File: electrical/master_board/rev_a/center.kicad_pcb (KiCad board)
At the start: 2 copper layers, 125 x 97.6 mm, 9 parts, among them CN50 HCSR04;F1X4, CN51 HCSR04LP;F1X4, CN52 HCSR04LP;F1X4, CN53 HCSR04LP;F1X4, CN54 HCSR04;F1X4, CN55 HR2_EncoderMate;2XF1X3, CN56 HR2_EncoderMate;2XF1X3, CN57 RASPI;F2X20, CN58 ST_MATE;ST_MATE

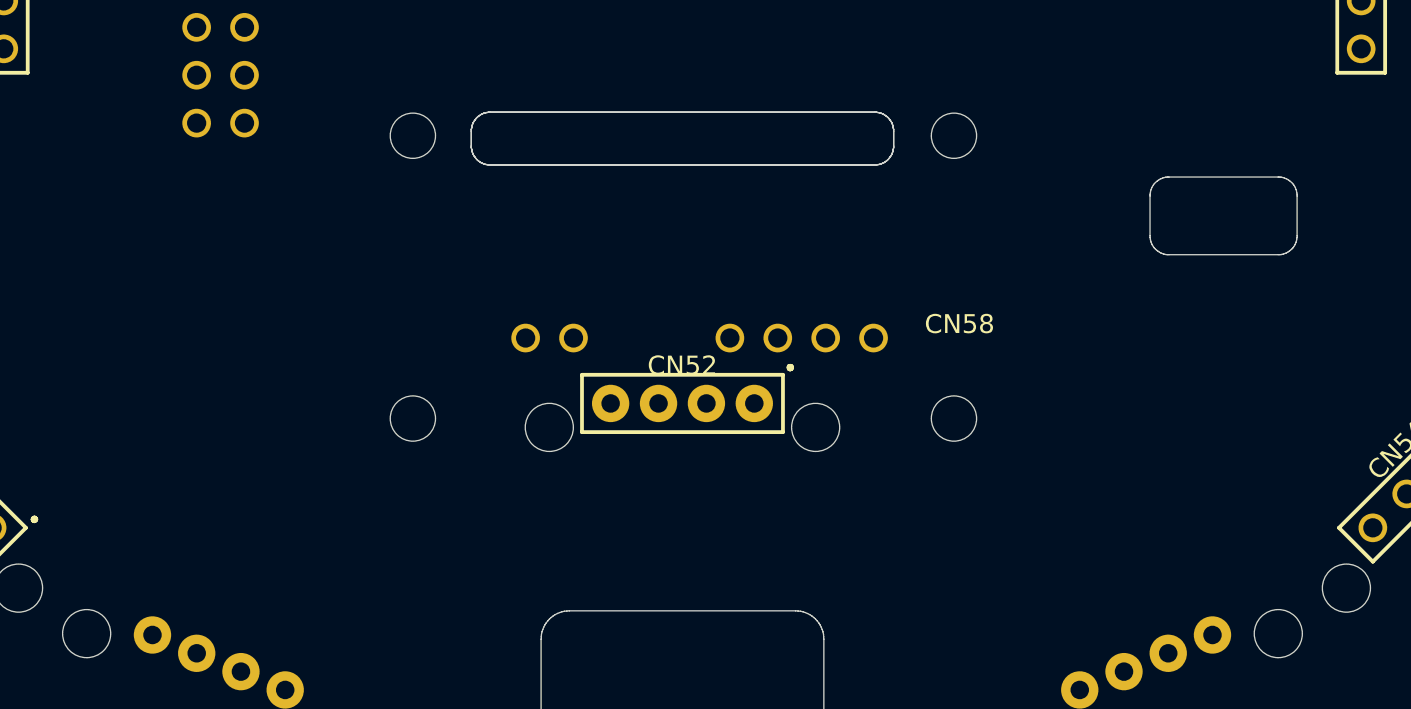
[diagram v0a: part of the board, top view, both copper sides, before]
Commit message: ST Mate is automatically placed on the center.kicad_pcb.
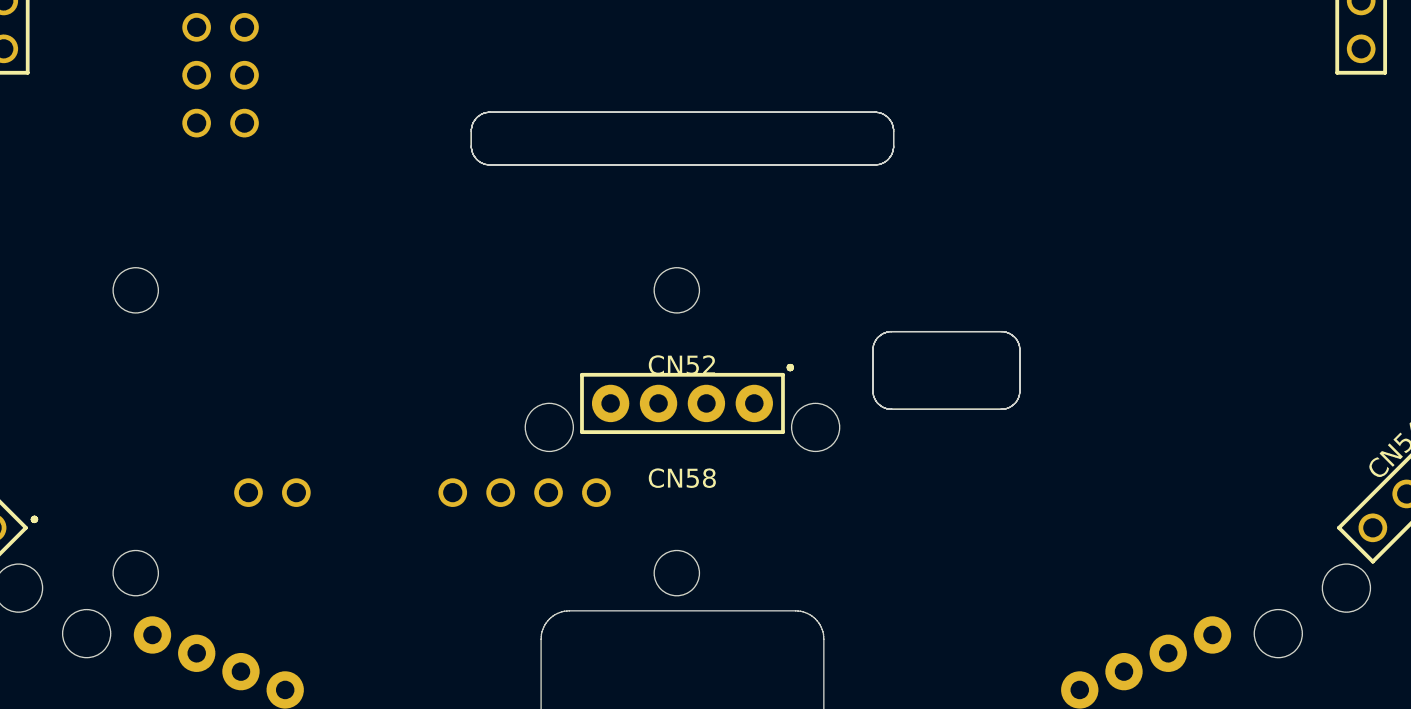
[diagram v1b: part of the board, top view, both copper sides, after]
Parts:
- moved CN58 16.8 mm to (100.0, 145.0)
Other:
- outline, holes or cut-outs redrawn
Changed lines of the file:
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@@
   )
   (module HR2:ST_MATE (layer F.Cu)
-    (at 114.7 136.8)
+    (at 100 145)
     (fp_text reference CN58 (at 0 -2) (layer F.SilkS)
       (effects (font (size 1 1) (thickness 0.2)))
@@
       (net 8 "Net-(CN52-Pad1)"))
   )
+  (gr_line (start 117.9 136.19) (end 117.9 136.1) (layer Edge.Cuts) (width 0.05))
+  (gr_line (start 117.9 136.1) (end 117.88 136.01) (layer Edge.Cuts) (width 0.05))
+  (gr_line (start 117.88 136.01) (end 117.87 135.93) (layer Edge.Cuts) (width 0.05))
+  (gr_line (start 117.87 135.93) (end 117.84 135.85) (layer Edge.Cuts) (width 0.05))
+  (gr_line (start 117.84 135.85) (end 117.81 135.76) (layer Edge.Cuts) (width 0.05))
+  (gr_line (start 117.81 135.76) (end 117.77 135.69) (layer Edge.Cuts) (width 0.05))
+  (gr_line (start 117.77 135.69) (end 117.72 135.61) (layer Edge.Cuts) (width 0.05))
+  (gr_line (start 117.72 135.61) (end 117.67 135.54) (layer Edge.Cuts) (width 0.05))
+  (gr_line (start 117.67 135.54) (end 117.61 135.48) (layer Edge.Cuts) (width 0.05))
+  (gr_line (start 117.61 135.48) (end 117.54 135.42) (layer Edge.Cuts) (width 0.05))
+  (gr_line (start 117.54 135.42) (end 117.47 135.37) (layer Edge.Cuts) (width 0.05))
+  (gr_line (start 117.47 135.37) (end 117.4 135.32) (layer Edge.Cuts) (width 0.05))
+  (gr_line (start 117.4 135.32) (end 117.32 135.28) (layer Edge.Cuts) (width 0.05))
+  (gr_line (start 117.32 135.28) (end 117.24 135.25) (layer Edge.Cuts) (width 0.05))
+  (gr_line (start 117.24 135.25) (end 117.16 135.22) (layer Edge.Cuts) (width 0.05))
+  (gr_line (start 117.16 135.22) (end 117.07 135.2) (layer Edge.Cuts) (width 0.05))
+  (gr_line (start 117.07 135.2) (end 116.99 135.19) (layer Edge.Cuts) (width 0.05))
+  (gr_line (start 116.99 135.19) (end 116.9 135.19) (layer Edge.Cuts) (width 0.05))
+  (gr_line (start 116.9 135.19) (end 111.1 135.19) (layer Edge.Cuts) (width 0.05))
+  (gr_line (start 111.1 135.19) (end 111.01 135.19) (layer Edge.Cuts) (width 0.05))
+  (gr_line (start 111.01 135.19) (end 110.93 135.2) (layer Edge.Cuts) (width 0.05))
+  (gr_line (start 110.93 135.2) (end 110.84 135.22) (layer Edge.Cuts) (width 0.05))
+  (gr_line (start 110.84 135.22) (end 110.76 135.25) (layer Edge.Cuts) (width 0.05))
+  (gr_line (start 110.76 135.25) (end 110.68 135.28) (layer Edge.Cuts) (width 0.05))
+  (gr_line (start 110.68 135.28) (end 110.6 135.32) (layer Edge.Cuts) (width 0.05))
+  (gr_line (start 110.6 135.32) (end 110.53 135.37) (layer Edge.Cuts) (width 0.05))
+  (gr_line (start 110.53 135.37) (end 110.46 135.42) (layer Edge.Cuts) (width 0.05))
+  (gr_line (start 110.46 135.42) (end 110.39 135.48) (layer Edge.Cuts) (width 0.05))
+  (gr_line (start 110.39 135.48) (end 110.33 135.54) (layer Edge.Cuts) (width 0.05))
+  (gr_line (start 110.33 135.54) (end 110.28 135.61) (layer Edge.Cuts) (width 0.05))
+  (gr_line (start 110.28 135.61) (end 110.23 135.69) (layer Edge.Cuts) (width 0.05))
+  (gr_line (start 110.23 135.69) (end 110.19 135.76) (layer Edge.Cuts) (width 0.05))
+  (gr_line (start 110.19 135.76) (end 110.16 135.85) (layer Edge.Cuts) (width 0.05))
+  (gr_line (start 110.16 135.85) (end 110.13 135.93) (layer Edge.Cuts) (width 0.05))
+  (gr_line (start 110.13 135.93) (end 110.12 136.01) (layer Edge.Cuts) (width 0.05))
+  (gr_line (start 110.12 136.01) (end 110.1 136.1) (layer Edge.Cuts) (width 0.05))
+  (gr_line (start 110.1 136.1) (end 110.1 136.19) (layer Edge.Cuts) (width 0.05))
+  (gr_line (start 110.1 136.19) (end 110.1 138.31) (layer Edge.Cuts) (width 0.05))
+  (gr_line (start 110.1 138.31) (end 110.1 138.4) (layer Edge.Cuts) (width 0.05))
+  (gr_line (start 110.1 138.4) (end 110.12 138.49) (layer Edge.Cuts) (width 0.05))
+  (gr_line (start 110.12 138.49) (end 110.13 138.57) (layer Edge.Cuts) (width 0.05))
+  (gr_line (start 110.13 138.57) (end 110.16 138.65) (layer Edge.Cuts) (width 0.05))
+  (gr_line (start 110.16 138.65) (end 110.19 138.74) (layer Edge.Cuts) (width 0.05))
+  (gr_line (start 110.19 138.74) (end 110.23 138.81) (layer Edge.Cuts) (width 0.05))
+  (gr_line (start 110.23 138.81) (end 110.28 138.89) (layer Edge.Cuts) (width 0.05))
+  (gr_line (start 110.28 138.89) (end 110.33 138.96) (layer Edge.Cuts) (width 0.05))
+  (gr_line (start 110.33 138.96) (end 110.39 139.02) (layer Edge.Cuts) (width 0.05))
+  (gr_line (start 110.39 139.02) (end 110.46 139.08) (layer Edge.Cuts) (width 0.05))
+  (gr_line (start 110.46 139.08) (end 110.53 139.13) (layer Edge.Cuts) (width 0.05))
+  (gr_line (start 110.53 139.13) (end 110.6 139.18) (layer Edge.Cuts) (width 0.05))
+  (gr_line (start 110.6 139.18) (end 110.68 139.22) (layer Edge.Cuts) (width 0.05))
+  (gr_line (start 110.68 139.22) (end 110.76 139.25) (layer Edge.Cuts) (width 0.05))
+  (gr_line (start 110.76 139.25) (end 110.84 139.28) (layer Edge.Cuts) (width 0.05))
+  (gr_line (start 110.84 139.28) (end 110.93 139.3) (layer Edge.Cuts) (width 0.05))
+  (gr_line (start 110.93 139.3) (end 111.01 139.31) (layer Edge.Cuts) (width 0.05))
+  (gr_line (start 111.01 139.31) (end 111.1 139.31) (layer Edge.Cuts) (width 0.05))
+  (gr_line (start 111.1 139.31) (end 116.9 139.31) (layer Edge.Cuts) (width 0.05))
+  (gr_line (start 116.9 139.31) (end 116.99 139.31) (layer Edge.Cuts) (width 0.05))
+  (gr_line (start 116.99 139.31) (end 117.07 139.3) (layer Edge.Cuts) (width 0.05))
+  (gr_line (start 117.07 139.3) (end 117.16 139.28) (layer Edge.Cuts) (width 0.05))
+  (gr_line (start 117.16 139.28) (end 117.24 139.25) (layer Edge.Cuts) (width 0.05))
+  (gr_line (start 117.24 139.25) (end 117.32 139.22) (layer Edge.Cuts) (width 0.05))
+  (gr_line (start 117.32 139.22) (end 117.4 139.18) (layer Edge.Cuts) (width 0.05))
+  (gr_line (start 117.4 139.18) (end 117.47 139.13) (layer Edge.Cuts) (width 0.05))
+  (gr_line (start 117.47 139.13) (end 117.54 139.08) (layer Edge.Cuts) (width 0.05))
+  (gr_line (start 117.54 139.08) (end 117.61 139.02) (layer Edge.Cuts) (width 0.05))
+  (gr_line (start 117.61 139.02) (end 117.67 138.96) (layer Edge.Cuts) (width 0.05))
+  (gr_line (start 117.67 138.96) (end 117.72 138.89) (layer Edge.Cuts) (width 0.05))
+  (gr_line (start 117.72 138.89) (end 117.77 138.81) (layer Edge.Cuts) (width 0.05))
+  (gr_line (start 117.77 138.81) (end 117.81 138.74) (layer Edge.Cuts) (width 0.05))
+  (gr_line (start 117.81 138.74) (end 117.84 138.65) (layer Edge.Cuts) (width 0.05))
+  (gr_line (start 117.84 138.65) (end 117.87 138.57) (layer Edge.Cuts) (width 0.05))
+  (gr_line (start 117.87 138.57) (end 117.88 138.49) (layer Edge.Cuts) (width 0.05))
+  (gr_line (start 117.88 138.49) (end 117.9 138.4) (layer Edge.Cuts) (width 0.05))
+  (gr_line (start 117.9 138.4) (end 117.9 138.31) (layer Edge.Cuts) (width 0.05))
+  (gr_line (start 117.9 138.31) (end 117.9 136.19) (layer Edge.Cuts) (width 0.05))
   (gr_line (start 106.3 85) (end 106.21 85) (layer Edge.Cuts) (width 0.05))
   (gr_line (start 106.21 85) (end 106.13 85.02) (layer Edge.Cuts) (width 0.05))

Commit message: Finally have everything fitting together.
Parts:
- moved CN58 17.9 mm to (117.8, 147.0)
- moved CN50 9.21 mm to (64.9, 151.1)
- moved CN54 9.21 mm to (135.1, 151.1)
- moved CN51 3.92 mm to (73.9, 149.1)
- moved CN53 3.92 mm to (126.1, 149.1)
- moved CN52 1.00 mm to (100.0, 138.0)
- moved CN55 0.30 mm to (136.3, 100.0)
- moved CN56 0.30 mm to (63.7, 100.0)
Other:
- outline, holes or cut-outs redrawn

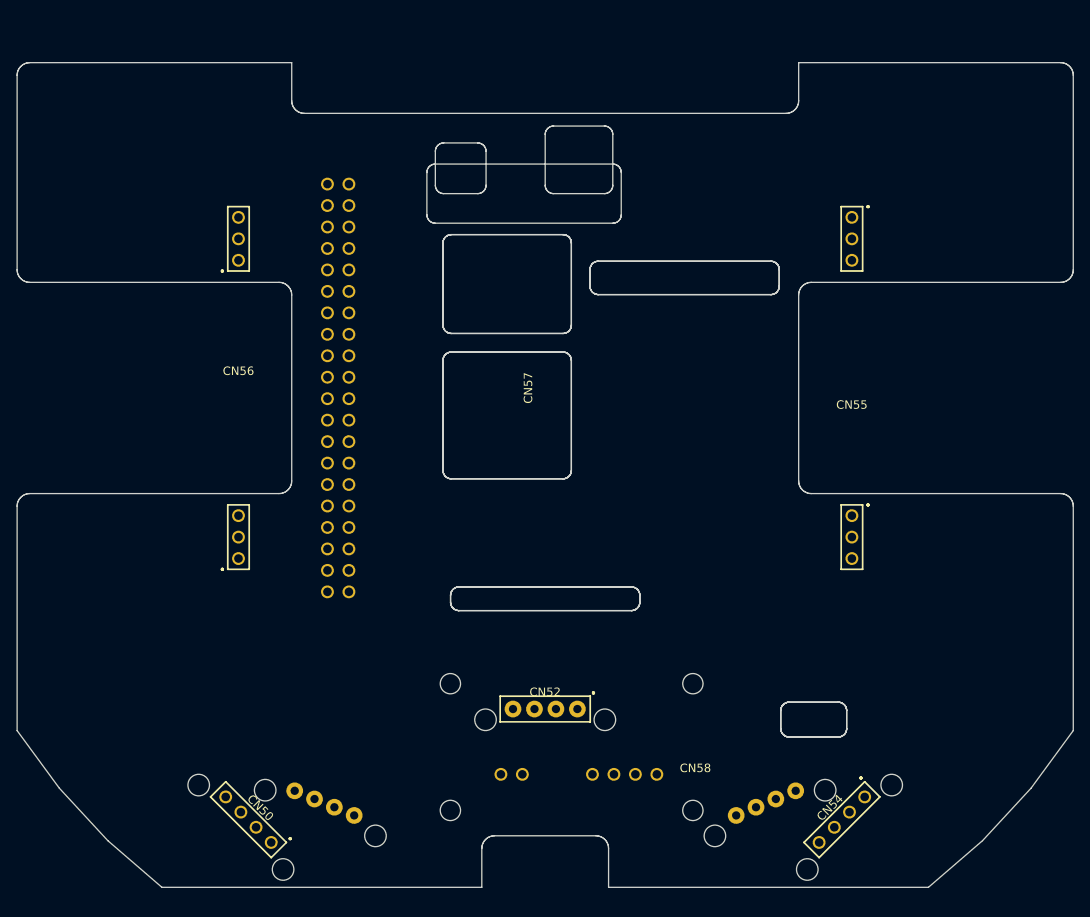
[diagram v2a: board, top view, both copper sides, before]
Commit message: Added spacer mounting holes to schematics and associated PCB's.
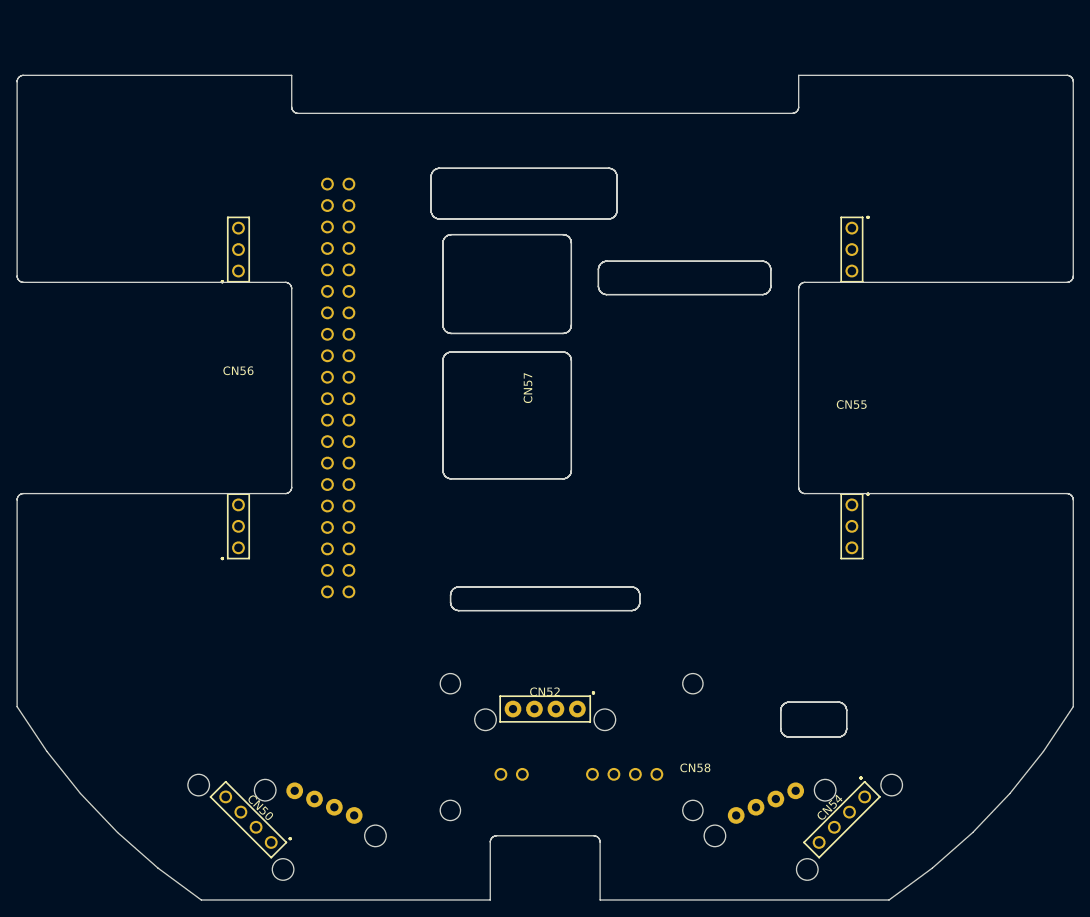
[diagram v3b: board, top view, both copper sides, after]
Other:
- outline, holes or cut-outs redrawn

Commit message: Placed all of the Groves on the PCB's.
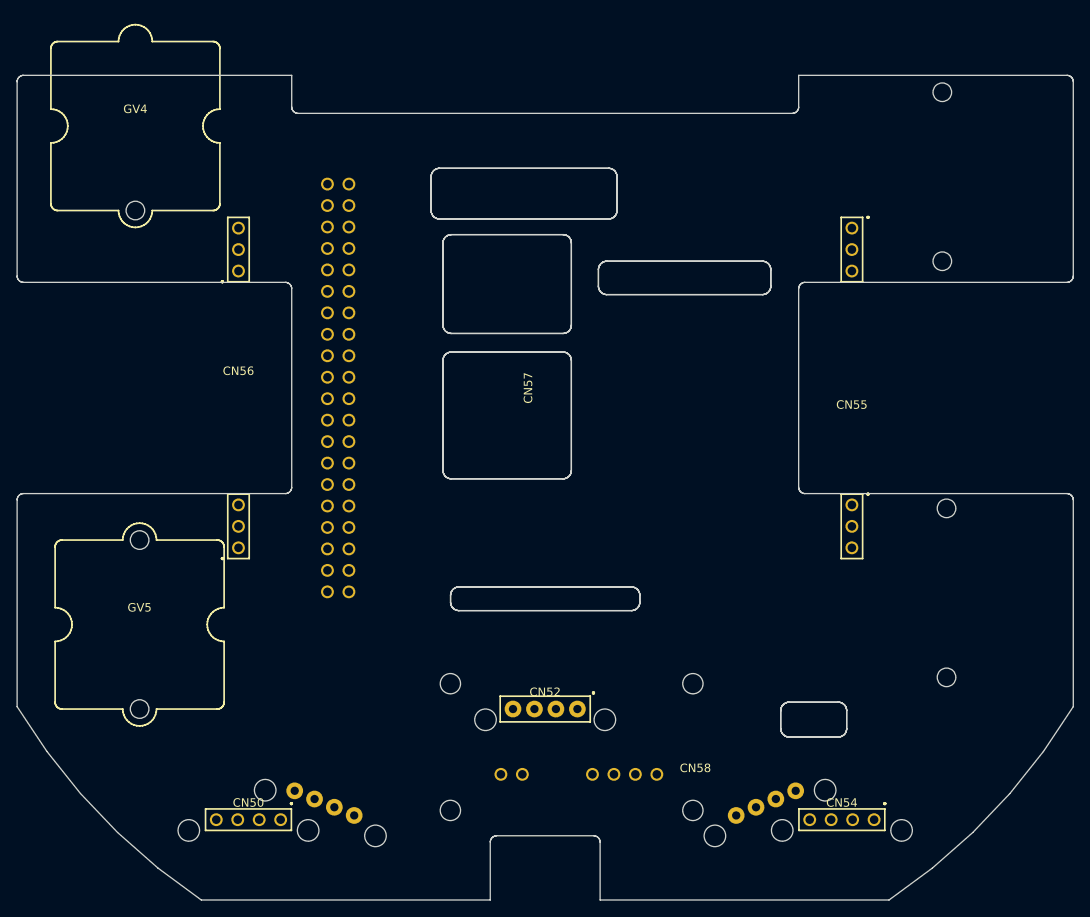
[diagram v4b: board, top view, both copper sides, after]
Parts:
- added GV3: GROVE;20x20, HR2:GROVE20x20, B.Cu at (147.0, 75.0)
- added GV4: GROVE;20x20L, HR2:GROVE20x20L, F.Cu at (51.5, 69.0)
- added GV5: GROVE;20x20, HR2:GROVE20x20, F.Cu at (52.0, 128.0)
- added GV6: GROVE;20x20, HR2:GROVE20x20, B.Cu at (147.5, 124.2)
- turned CN50 to 0 degrees
- turned CN54 to 0 degrees
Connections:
- CN50 pad 1: (no net) -> Net-(CN50-Pad1)
- CN50 pad 2: (no net) -> Net-(CN50-Pad2)
- CN50 pad 3: (no net) -> Net-(CN50-Pad3)
- CN50 pad 4: (no net) -> Net-(CN50-Pad4)
- CN54 pad 1: (no net) -> Net-(CN54-Pad1)
- CN54 pad 2: (no net) -> Net-(CN54-Pad2)
- CN54 pad 3: (no net) -> Net-(CN54-Pad3)
- CN54 pad 4: (no net) -> Net-(CN54-Pad4)

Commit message: Fixed Groves and added MikroBus's.
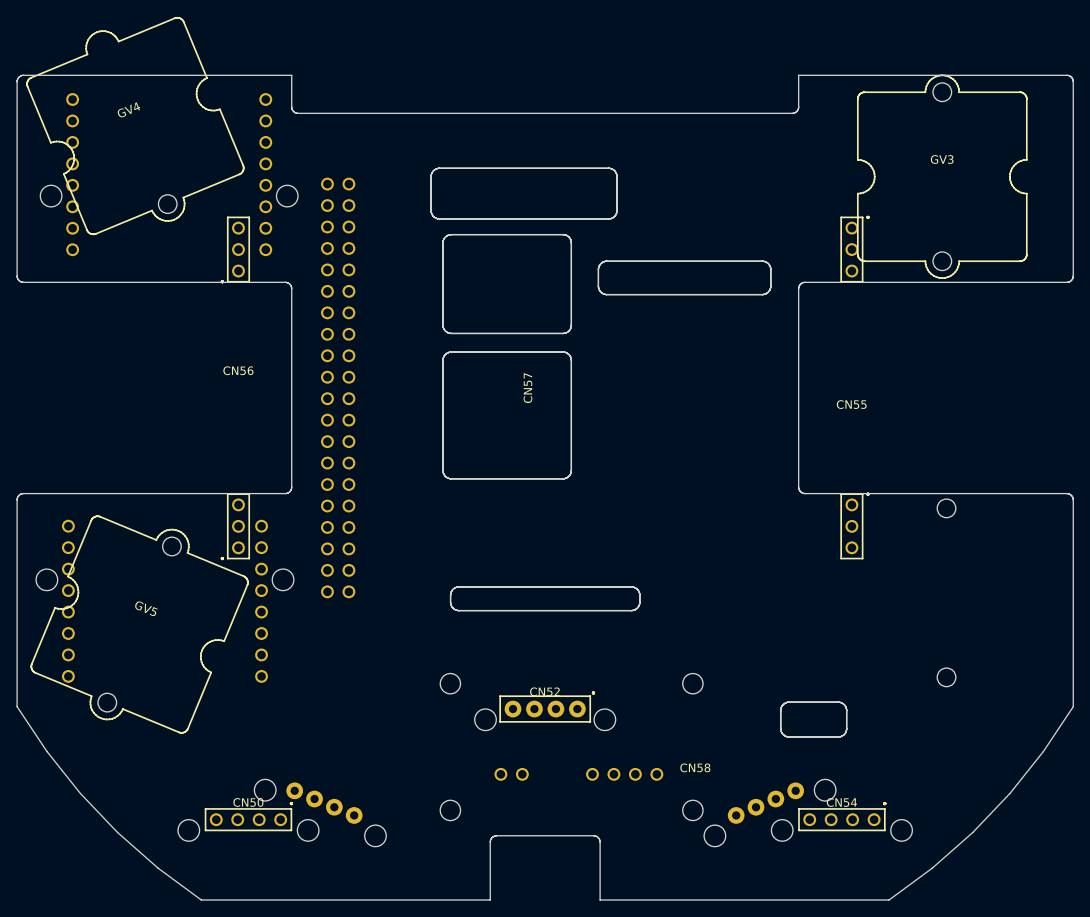
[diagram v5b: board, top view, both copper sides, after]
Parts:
- added CN40: MIKROBUS_MATE;SMALL, HR2:MIKROBUS_SMALL_MATE, B.Cu at (55.0, 125.2)
- added CN41: MIKROBUS_MATE;MEDIUM, HR2:MIKROBUS_MEDIUM_MATE, B.Cu at (55.5, 74.8)
- GV3: moved to F.Cu
- turned GV4 to 22.5 degrees
- turned GV5 to 337.5 degrees
